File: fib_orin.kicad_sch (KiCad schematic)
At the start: 8 parts, among them J1201 Orin Nano

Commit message: implemented most of USB and Power Supplies
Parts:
- C503: footprint Capacitor_SMD:C_0603_1608Metric -> Capacitor_SMD:C_0402_1005Metric
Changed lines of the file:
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@@
 			)
 		)
-		(property "Footprint" "Capacitor_SMD:C_0603_1608Metric"
+		(property "Footprint" "Capacitor_SMD:C_0402_1005Metric"
 			(at 355.6 236.22 0)
 			(effects

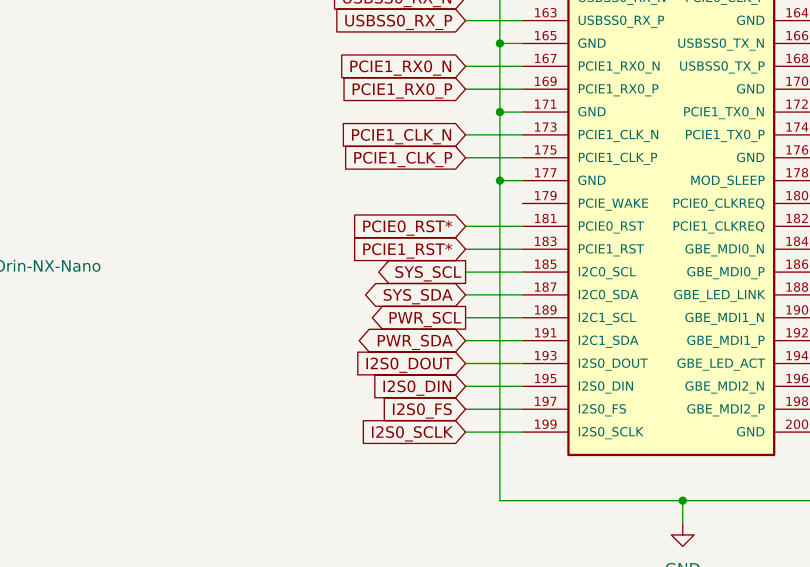
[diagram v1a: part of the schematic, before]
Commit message: 90 percent done with routing. need to go over all schematic pages, double check everything thoroughly, do lengthmatching add any missing footprints, take care of startup, ferrites, audio, eink connectors, 40pin header connections, rtc
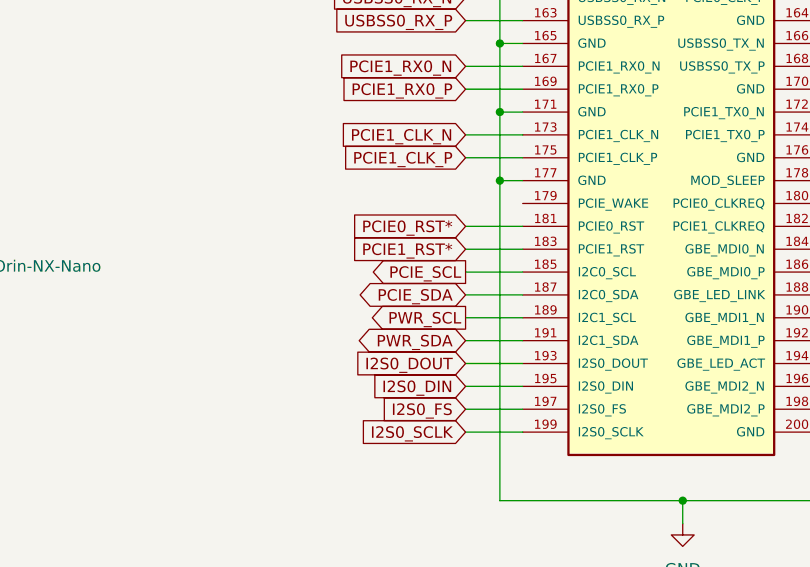
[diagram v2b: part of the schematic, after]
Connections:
- net SYS_SCL renamed PCIE_SCL
- net SYS_SDA renamed PCIE_SDA
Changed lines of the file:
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@@
 		)
 	)
-	(global_label "SYS_SCL"
+	(global_label "PCIE_SCL"
 		(shape output)
 		(at 261.62 106.68 180)
@@
 		)
 	)
-	(global_label "SYS_SDA"
+	(global_label "PCIE_SDA"
 		(shape bidirectional)
 		(at 261.62 109.22 180)

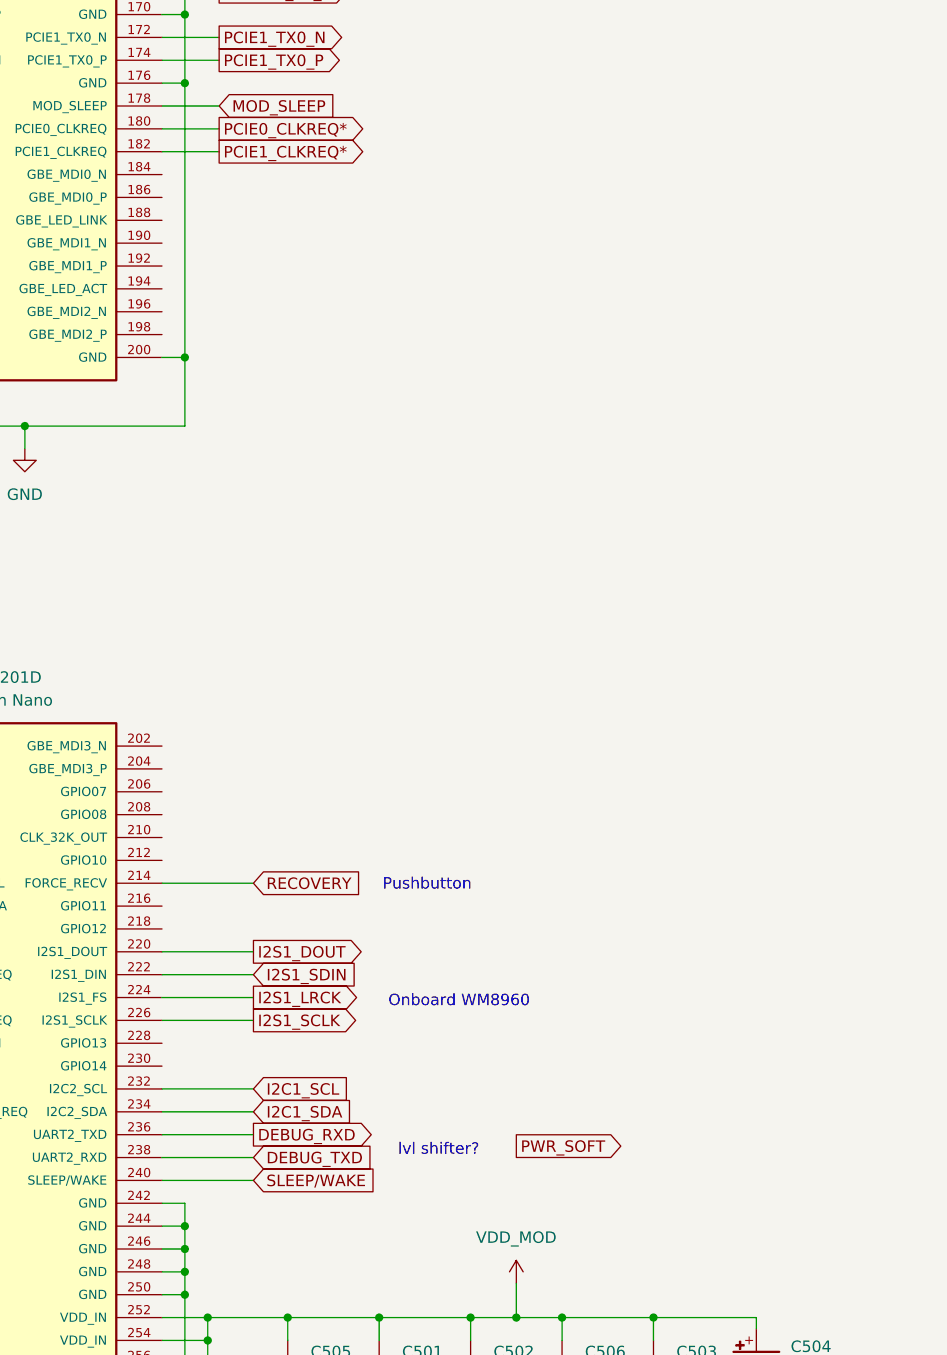
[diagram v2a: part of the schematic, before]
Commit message: replaced 1v8 buck with ldo, added startup circuit, added footprints for eink connectors
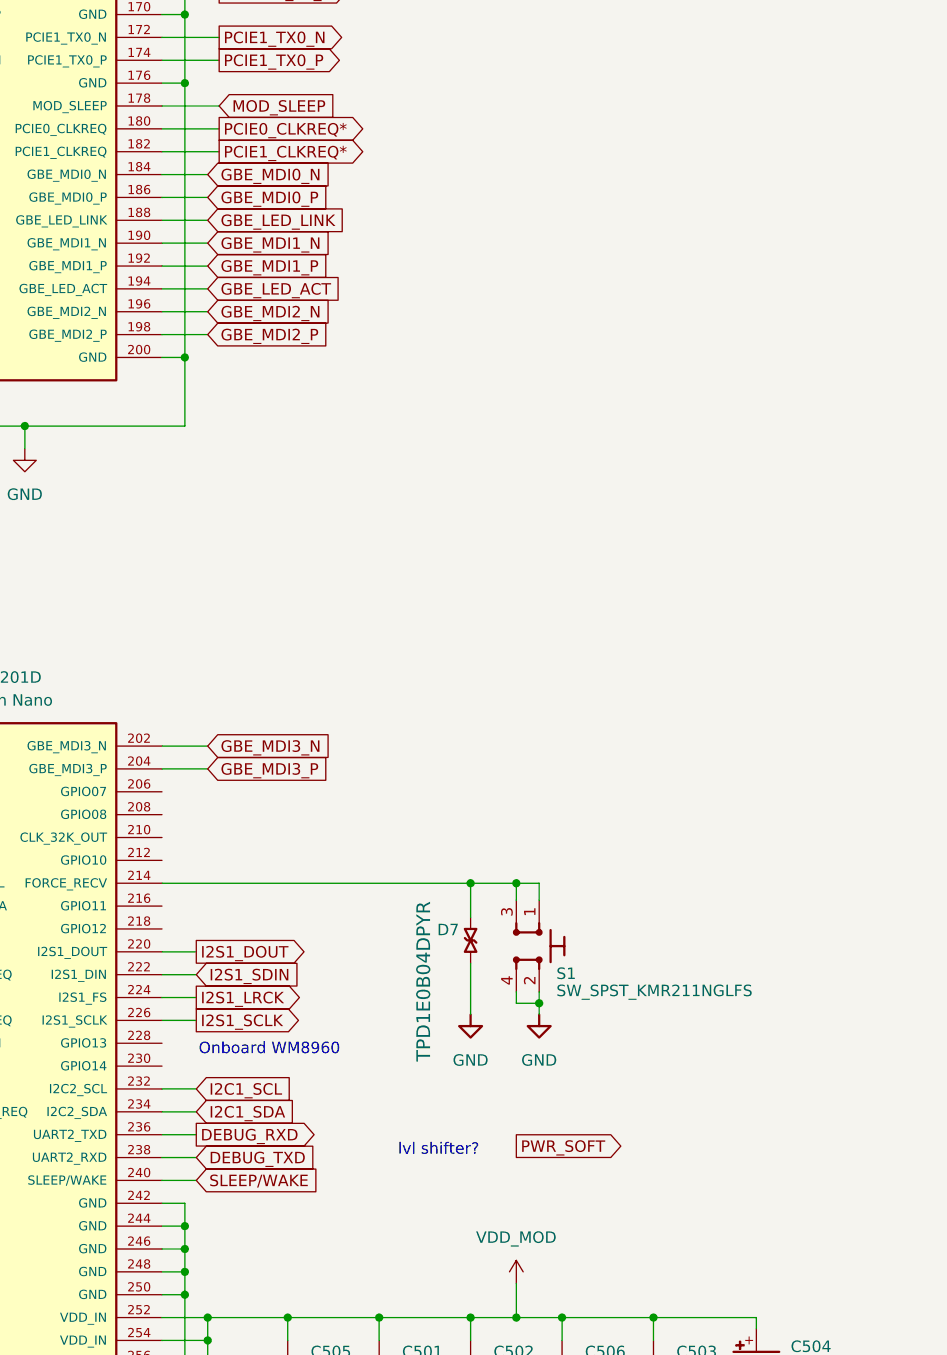
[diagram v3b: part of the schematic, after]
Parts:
- added D7: TPD1E0B04_XDFN-2, antmicro-footprints:XDFN-2_1x0.60mm, symbol antmicroTVSDiodes:TPD1E0B04_XDFN-2
- added S1: SW_SPST_KMR211NGLFS, antmicro-footprints:SW_KMR211NGLFS_SMD, symbol antmicroPushbuttonSwitches:SW_KMR211NGLFS_SMD
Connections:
- net GND: now also D7.1, S1.2, S1.4
- net GBE_MDI3_N: now reaches J1201.202 (GBE_MDI3_N)
- net GBE_MDI3_P: now reaches J1201.204 (GBE_MDI3_P)
- net GBE_MDI0_N: now reaches J1201.184 (GBE_MDI0_N)
- net GBE_MDI0_P: now reaches J1201.186 (GBE_MDI0_P)
- net GBE_LED_LINK: now reaches J1201.188 (GBE_LED_LINK)
- net GBE_MDI1_N: now reaches J1201.190 (GBE_MDI1_N)
- net GBE_MDI1_P: now reaches J1201.192 (GBE_MDI1_P)
- net GBE_LED_ACT: now reaches J1201.194 (GBE_LED_ACT)
- net GBE_MDI2_N: now reaches J1201.196 (GBE_MDI2_N)
- net GBE_MDI2_P: now reaches J1201.198 (GBE_MDI2_P)
- net RECOVERY: no longer names the net of J1201.214 (FORCE_RECV)
- net RECOVERY: now also D7.2, S1.1, S1.3
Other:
- note removed: "Pushbutton"

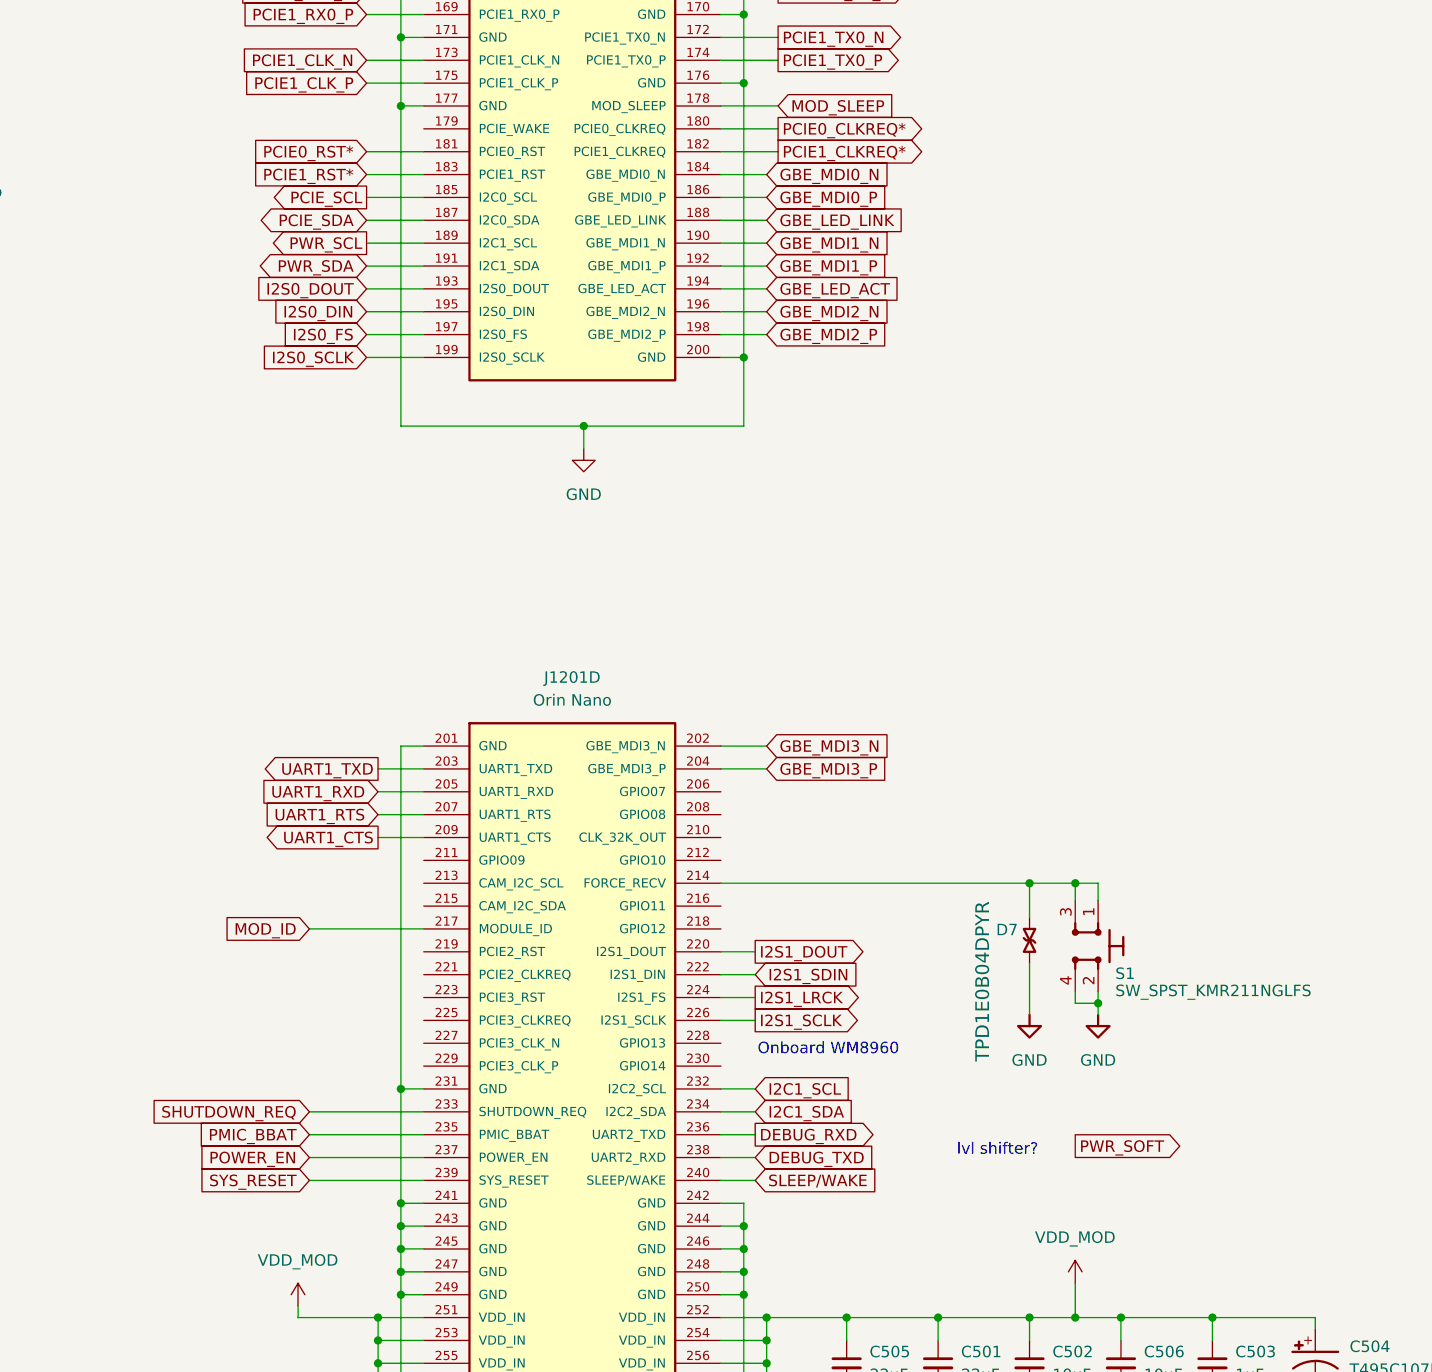
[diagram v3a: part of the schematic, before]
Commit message: added all missing footprints, fixed library & footprint links, did layout out 99% of components, all that's left is rtc(?), peripherals, routing & lengthmatching and final sanity checks
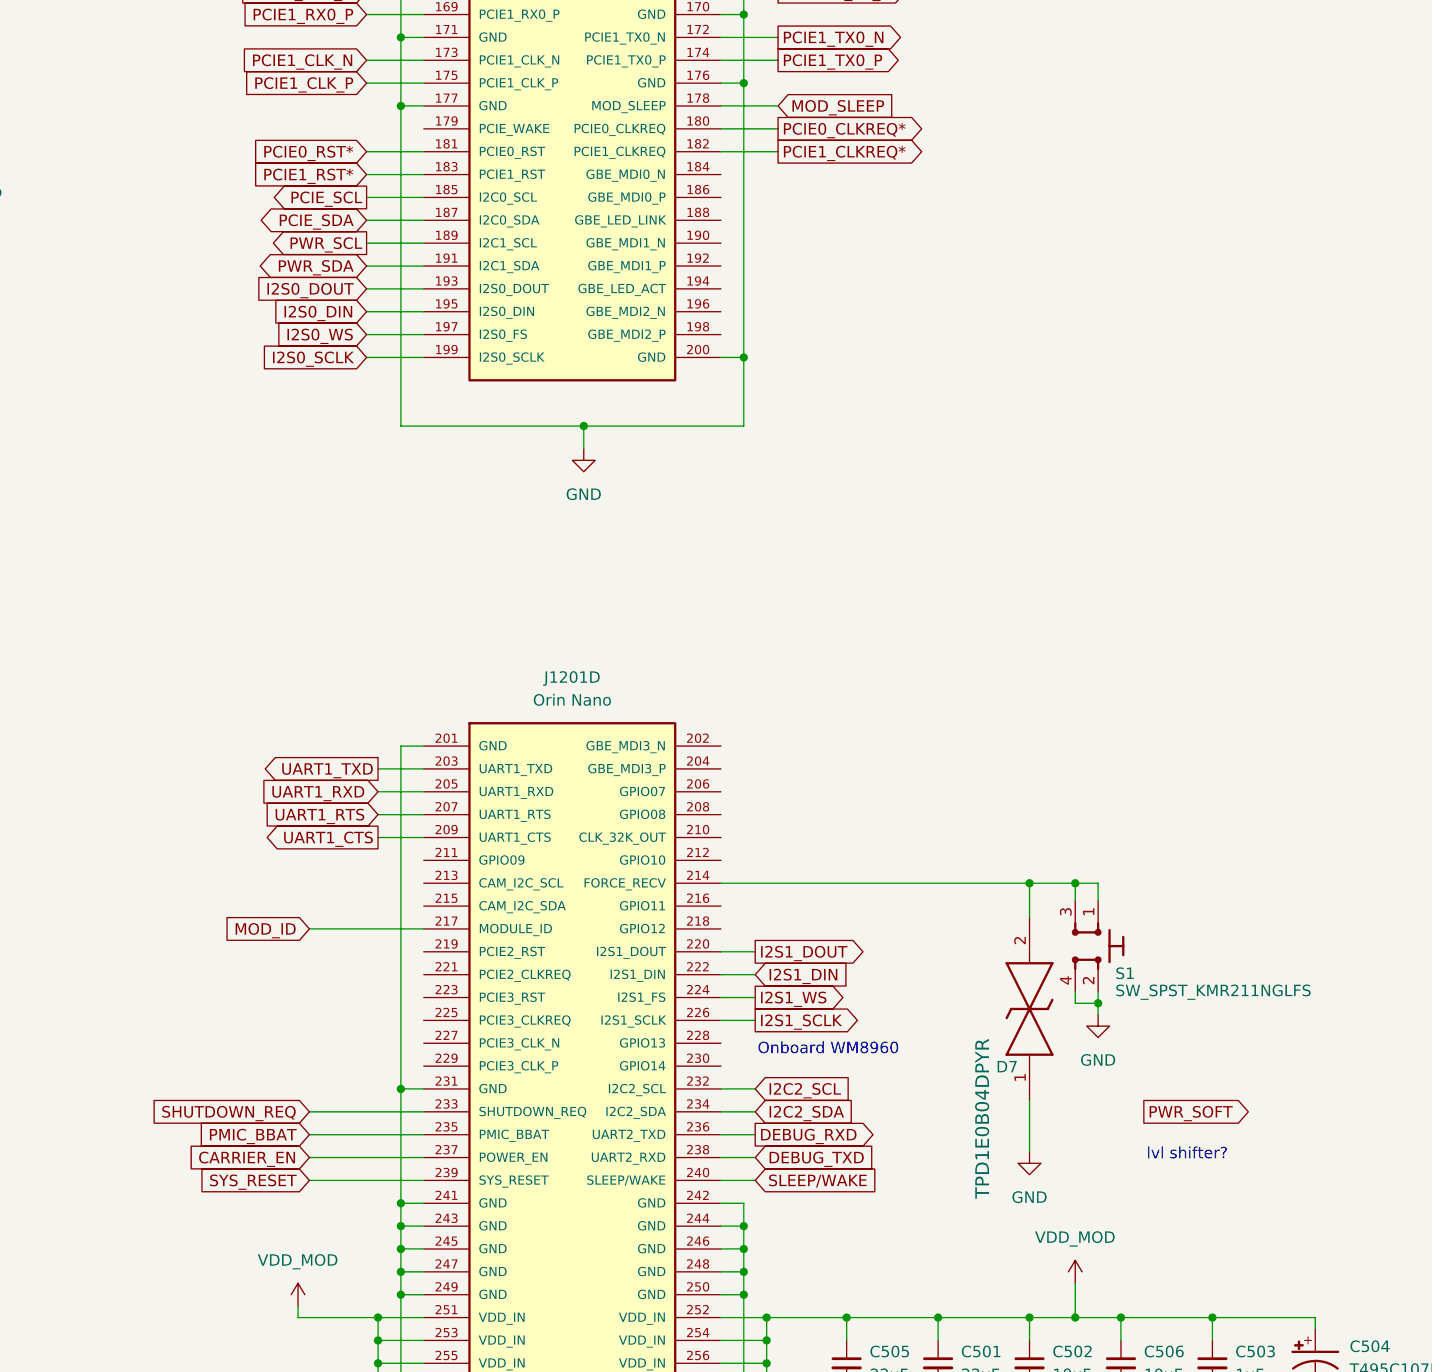
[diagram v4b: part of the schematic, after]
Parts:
- D7: footprint antmicro-footprints:XDFN-2_1x0.60mm -> TPD1E0B04DPYT; symbol antmicroTVSDiodes:TPD1E0B04_XDFN-2 -> Fibel2:TPD1E0B04DPYT; Height (none) -> 0.45; Manufacturer_Name (none) -> Texas Instruments; Manufacturer_Part_Number (none) -> TPD1E0B04DPYT; Mouser Part Number (none) -> 595-TPD1E0B04DPYT; Mouser Price/Stock (none) -> https://www.mouser.co.uk/ProductDetail/Texas-Instruments/TP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
- S1: footprint antmicro-footprints:SW_KMR211NGLFS_SMD -> Fibel2:KMR211NGLFS; symbol antmicroPushbuttonSwitches:SW_KMR211NGLFS_SMD -> Fibel2:SW_KMR211NGLFS_SMD
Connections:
- net GBE_LED_ACT: no longer names the net of J1201.194 (GBE_LED_ACT)
- net GBE_LED_LINK: no longer names the net of J1201.188 (GBE_LED_LINK)
- net GBE_MDI0_N: no longer names the net of J1201.184 (GBE_MDI0_N)
- net GBE_MDI0_P: no longer names the net of J1201.186 (GBE_MDI0_P)
- net GBE_MDI1_N: no longer names the net of J1201.190 (GBE_MDI1_N)
- net GBE_MDI1_P: no longer names the net of J1201.192 (GBE_MDI1_P)
- net GBE_MDI2_N: no longer names the net of J1201.196 (GBE_MDI2_N)
- net GBE_MDI2_P: no longer names the net of J1201.198 (GBE_MDI2_P)
- net GBE_MDI3_N: no longer names the net of J1201.202 (GBE_MDI3_N)
- net GBE_MDI3_P: no longer names the net of J1201.204 (GBE_MDI3_P)
- net I2C1_SCL renamed I2C2_SCL
- net I2C1_SDA renamed I2C2_SDA
- net I2S0_FS renamed I2S0_WS
- net I2S1_LRCK renamed I2S1_WS
- net I2S1_SDIN renamed I2S1_DIN
- net POWER_EN renamed CARRIER_EN

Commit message: did length tuning, routing of final submodules and most of power routing
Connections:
- net GND: now also S1.3; no longer S1.4
- net at D7.2, J1201.214 (FORCE_RECV), S1.1: now also S1.4; no longer S1.3
- net SHUTDOWN_REQ renamed ~{SHUTDOWN_REQ}
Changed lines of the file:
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@@
 		)
 	)
-	(global_label "SHUTDOWN_REQ"
+	(global_label "~{SHUTDOWN_REQ}"
 		(shape input)
 		(at 255.27 208.28 180)

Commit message: added port expander and level shifters, routed peripherals fixed most drc errors, assigned gpios etc.
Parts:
- added C42, C43, C44, C45, C46, C47, C50, C51: 100nF, Capacitor_SMD:C_0402_1005Metric, symbol Fibel2:C_Small_Rota
- added IC5, IC6, IC7, IC9: TXB0108RGYR, Fibel2:TXB0108, symbol Fibel2:TXB0108RGYR
- D7: footprint TPD1E0B04DPYT -> Fibel2:TPD1E0B04DPYT
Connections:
- net CARRIER_EN: now also IC5.10 (OE), IC6.10 (OE), IC7.10 (OE), IC9.10 (OE)
- net GND: now also C42.2, C43.2, C44.2, C45.2, C46.2, C47.2, C50.2, C51.2, IC5.11 (GND), IC5.21 (EP), IC6.11 (GND), IC6.21 (EP), IC7.11 (GND), IC7.21 (EP), IC9.11 (GND), IC9.21 (EP)
- net GPIO010: now also J1201.212 (GPIO10), IC7.7 (A6)
- net I2C2_SCL: now also IC5.1 (A1)
- net I2C2_SDA: now also IC5.3 (A2)
- net I2S0_DIN: now also IC6.4 (A3)
- net I2S0_DOUT: now also IC6.5 (A4)
- net I2S0_SCLK: now also IC6.1 (A1)
- net I2S0_WS: now also IC6.3 (A2)
- net IT8951_HRDY: now also J1201.230 (GPIO14), IC9.3 (A2)
- net IT8951_RST: now also J1201.228 (GPIO13), IC9.4 (A3)
- net IT8951_SPI1_CS0: now also IC9.8 (A7)
- net IT8951_SPI1_MISO: now also IC9.6 (A5)
- net IT8951_SPI1_MOSI: now also IC9.7 (A6)
- net IT8951_SPI1_SCK: now also IC9.5 (A4)
- net SPI0_CS0: now also IC5.7 (A6)
- net SPI0_CS1: now also IC5.8 (A7)
- net SPI0_MISO: now also IC5.5 (A4)
- net SPI0_MOSI: now also IC5.4 (A3)
- net SPI0_SCK: now also IC5.6 (A5)
- net UART1_CTS: now also IC6.9 (A8)
- net UART1_RTS: now also IC6.8 (A7)
- net UART1_RXD: now also IC6.7 (A6)
- net UART1_TXD: now also IC6.6 (A5)
- net GPIO001: now reaches J1201.118 (GPIO01)
- net GPIO001: now also IC7.4 (A3)
- net GPIO000: now reaches J1201.87 (GPIO00)
- net GPIO000: now also IC7.3 (A2)
- net GPIO007: now reaches J1201.206 (GPIO07)
- net GPIO008: now reaches J1201.208 (GPIO08)
- net GPIO008: now also IC7.8 (A7)
- net GPIO009: now reaches J1201.211 (GPIO09)
- net GPIO009: now also IC7.9 (A8)
- net GPIO011: now reaches J1201.216 (GPIO11)
- net GPIO011: now also IC7.6 (A5)
- net GPIO012: now reaches J1201.218 (GPIO12)
- net GPIO012: now also IC7.5 (A4)
- net PCIE_WAKE*: now reaches J1201.179 (PCIE_WAKE)
- new net +1V8: C42.1, C44.1, C46.1, C50.1, IC5.2 (VCCA), IC6.2 (VCCA), IC7.2 (VCCA), IC9.2 (VCCA)
- new net +3V3: C43.1, C45.1, C47.1, C51.1, IC5.19 (VCCB), IC6.19 (VCCB), IC7.19 (VCCB), IC9.19 (VCCB)
- new net I2C2_SCL_3V: IC5.20 (B1)
- new net I2C2_SDA_3V: IC5.18 (B2)
- new net I2S0_3V3_DIN: IC6.17 (B3)
- new net I2S0_3V3_DOUT: IC6.16 (B4)
- new net I2S0_3V3_SCLK: IC6.20 (B1)
- new net I2S0_3V3_WS: IC6.18 (B2)
- new net IT8951_HRDY_3V3: IC9.18 (B2)
- new net IT8951_RST_3V3: IC9.17 (B3)
- new net IT8951_SPI1_CS0_3V3: IC9.13 (B7)
- new net IT8951_SPI1_MISO_3V3: IC9.14 (B6)
- new net IT8951_SPI1_MOSI_3V3: IC9.15 (B5)
- new net IT8951_SPI1_SCK_3V3: IC9.16 (B4)
- new net RP_GPIO04: IC7.18 (B2)
- new net RP_GPIO17: IC7.17 (B3)
- new net RP_GPIO22: IC7.15 (B5)
- new net RP_GPIO23: IC7.14 (B6)
- new net RP_GPIO24: IC7.13 (B7)
- new net RP_GPIO25: IC7.12 (B8)
- new net RP_GPIO27: IC7.16 (B4)
- new net SPI0_3V3_CS0: IC5.14 (B6)
- new net SPI0_3V3_CS1: IC5.13 (B7)
- new net SPI0_3V3_MISO: IC5.16 (B4)
- new net SPI0_3V3_MOSI: IC5.17 (B3)
- new net SPI0_3V3_SCK: IC5.15 (B5)
- new net UART1_3V3_CTS: IC6.12 (B8)
- new net UART1_3V3_RTS: IC6.13 (B7)
- new net UART1_3V3_RXD: IC6.14 (B6)
- new net UART1_3V3_TXD: IC6.15 (B5)
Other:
- note added: "might need gpio swap"
- note removed: "lvl shifter?"
- moved on the sheet: A501, C501, C502, C503, C504, C505, C506, D7, J1201A, J1201B, J1201C, J1201D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
